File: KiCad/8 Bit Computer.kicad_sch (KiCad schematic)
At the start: 26 parts, among them J1 USB_B

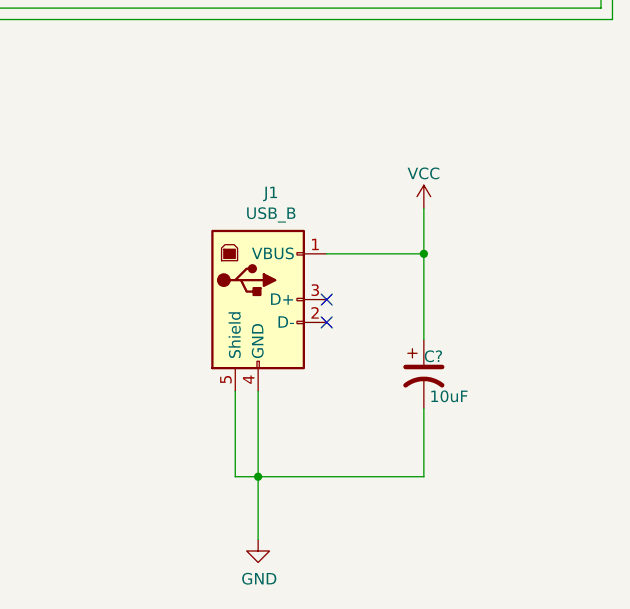
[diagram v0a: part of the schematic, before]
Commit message: Added Power LED
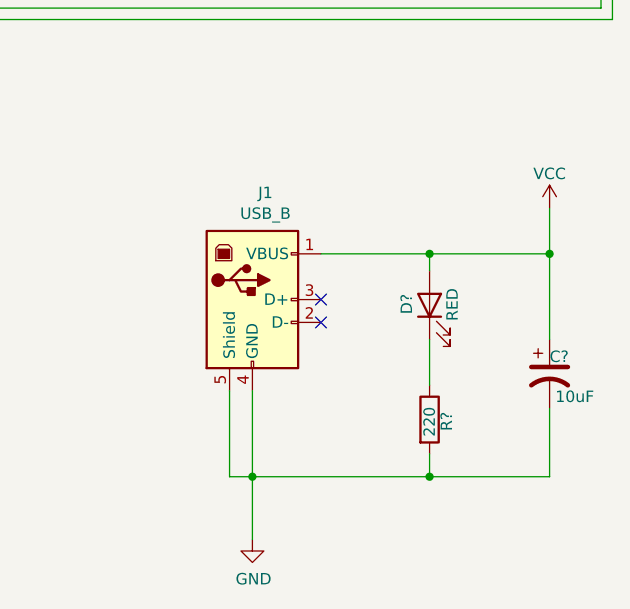
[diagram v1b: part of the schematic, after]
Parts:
- added D?: RED, LED_THT:LED_D5.0mm, symbol Device:LED
- added R?: 220, Resistor_THT:R_Axial_DIN0207_L6.3mm_D2.5mm_P7.62mm_Horizontal, symbol Device:R
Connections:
- net GND: now also R?.2
- net VCC: now also D?.2 (A)
- new net: D?.1 (K), R?.1
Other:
- moved on the sheet: C?, J1

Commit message: Updates
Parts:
- gave numbers to parts that had none: 27
